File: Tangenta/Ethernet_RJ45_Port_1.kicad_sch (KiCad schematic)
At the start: 1 part, among them J5 HY911130A

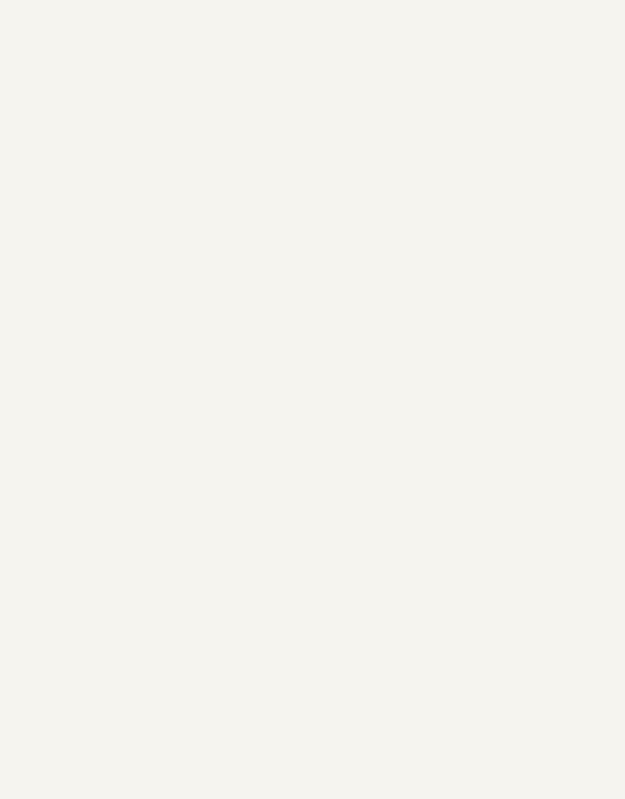
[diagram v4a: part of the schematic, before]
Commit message: Ethernet Switch schematic done, ports TBD...
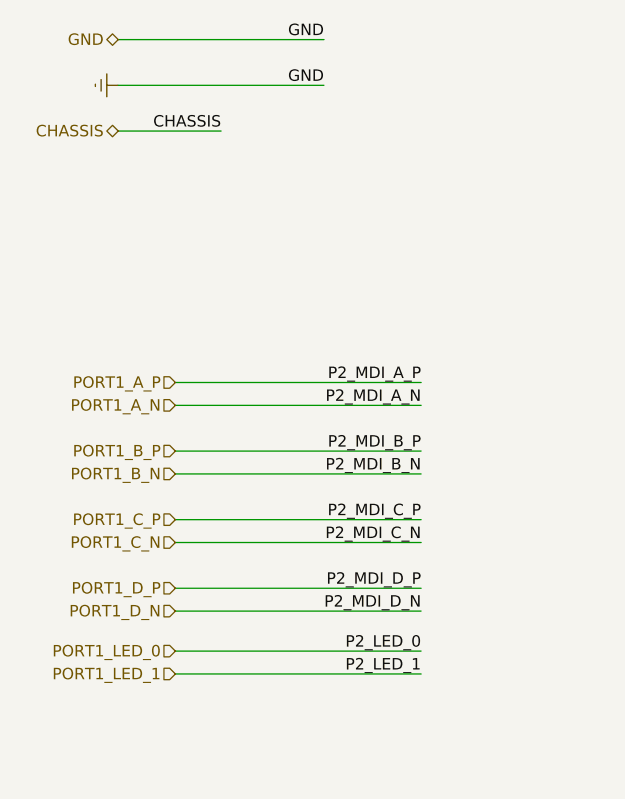
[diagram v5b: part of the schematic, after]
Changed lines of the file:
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@@
   (no_connect (at 134.62 75.565))
   (no_connect (at 160.02 73.025))
+  (wire (pts (xy 59.055 74.93) (xy 31.75 74.93))
+    (stroke (width 0) (type default))
+  )
+  (wire (pts (xy 25.4 29.21) (xy 36.83 29.21))
+    (stroke (width 0) (type default))
+  )
+  (wire (pts (xy 59.055 86.995) (xy 31.75 86.995))
+    (stroke (width 0) (type default))
+  )
+  (wire (pts (xy 48.26 24.13) (xy 25.4 24.13))
+    (stroke (width 0) (type default))
+  )
+  (wire (pts (xy 59.055 59.69) (xy 31.75 59.69))
+    (stroke (width 0) (type default))
+  )
+  (wire (pts (xy 59.055 89.535) (xy 31.75 89.535))
+    (stroke (width 0) (type default))
+  )
+  (wire (pts (xy 59.055 72.39) (xy 31.75 72.39))
+    (stroke (width 0) (type default))
+  )
+  (wire (pts (xy 59.055 80.01) (xy 31.75 80.01))
+    (stroke (width 0) (type default))
+  )
+  (wire (pts (xy 59.055 57.15) (xy 31.75 57.15))
+    (stroke (width 0) (type default))
+  )
+  (wire (pts (xy 59.055 82.55) (xy 31.75 82.55))
+    (stroke (width 0) (type default))
+  )
+  (wire (pts (xy 59.055 64.77) (xy 31.75 64.77))
+    (stroke (width 0) (type default))
+  )
+  (wire (pts (xy 48.26 19.05) (xy 25.4 19.05))
+    (stroke (width 0) (type default))
+  )
+  (wire (pts (xy 59.055 67.31) (xy 31.75 67.31))
+    (stroke (width 0) (type default))
+  )
+  (label "P2_MDI_C_P" (at 59.055 72.39 180) (fields_autoplaced)
+    (effects (font (size 1.27 1.27)) (justify right bottom))
+  )
+  (label "P2_LED_1" (at 59.055 89.535 180) (fields_autoplaced)
+    (effects (font (size 1.27 1.27)) (justify right bottom))
+  )
+  (label "P2_MDI_D_N" (at 59.055 82.55 180) (fields_autoplaced)
+    (effects (font (size 1.27 1.27)) (justify right bottom))
+  )
+  (label "P2_MDI_C_N" (at 59.055 74.93 180) (fields_autoplaced)
+    (effects (font (size 1.27 1.27)) (justify right bottom))
+  )
+  (label "P2_MDI_A_N" (at 59.055 59.69 180) (fields_autoplaced)
+    (effects (font (size 1.27 1.27)) (justify right bottom))
+  )
+  (label "P2_LED_0" (at 59.055 86.995 180) (fields_autoplaced)
+    (effects (font (size 1.27 1.27)) (justify right bottom))
+  )
+  (label "P2_MDI_D_P" (at 59.055 80.01 180) (fields_autoplaced)
+    (effects (font (size 1.27 1.27)) (justify right bottom))
+  )
+  (label "P2_MDI_A_P" (at 59.055 57.15 180) (fields_autoplaced)
+    (effects (font (size 1.27 1.27)) (justify right bottom))
+  )
+  (label "GND" (at 48.26 24.13 180) (fields_autoplaced)
+    (effects (font (size 1.27 1.27)) (justify right bottom))
+  )
+  (label "GND" (at 48.26 19.05 180) (fields_autoplaced)
+    (effects (font (size 1.27 1.27)) (justify right bottom))
+  )
+  (label "P2_MDI_B_P" (at 59.055 64.77 180) (fields_autoplaced)
+    (effects (font (size 1.27 1.27)) (justify right bottom))
+  )
+  (label "P2_MDI_B_N" (at 59.055 67.31 180) (fields_autoplaced)
+    (effects (font (size 1.27 1.27)) (justify right bottom))
+  )
+  (label "CHASSIS" (at 36.83 29.21 180) (fields_autoplaced)
+    (effects (font (size 1.27 1.27)) (justify right bottom))
+  )
+  (hierarchical_label "GND" (shape bidirectional) (at 25.4 19.05 180) (fields_autoplaced)
+    (effects (font (size 1.27 1.27)) (justify right))
+  )
+  (hierarchical_label "PORT1_D_N" (shape input) (at 31.75 82.55 180) (fields_autoplaced)
+    (effects (font (size 1.27 1.27)) (justify right))
+  )
+  (hierarchical_label "CHASSIS" (shape bidirectional) (at 25.4 29.21 180) (fields_autoplaced)
+    (effects (font (size 1.27 1.27)) (justify right))
+  )
+  (hierarchical_label "PORT1_D_P" (shape input) (at 31.75 80.01 180) (fields_autoplaced)
+    (effects (font (size 1.27 1.27)) (justify right))
+  )
+  (hierarchical_label "PORT1_A_N" (shape input) (at 31.75 59.69 180) (fields_autoplaced)
+    (effects (font (size 1.27 1.27)) (justify right))
+  )
+  (hierarchical_label "PORT1_C_P" (shape input) (at 31.75 72.39 180) (fields_autoplaced)
+    (effects (font (size 1.27 1.27)) (justify right))
+  )
+  (hierarchical_label "PORT1_A_P" (shape input) (at 31.75 57.15 180) (fields_autoplaced)
+    (effects (font (size 1.27 1.27)) (justify right))
+  )
+  (hierarchical_label "PORT1_LED_0" (shape input) (at 31.75 86.995 180) (fields_autoplaced)
+    (effects (font (size 1.27 1.27)) (justify right))
+  )
+  (hierarchical_label "PORT1_B_P" (shape input) (at 31.75 64.77 180) (fields_autoplaced)
+    (effects (font (size 1.27 1.27)) (justify right))
+  )
+  (hierarchical_label "PORT1_B_N" (shape input) (at 31.75 67.31 180) (fields_autoplaced)
+    (effects (font (size 1.27 1.27)) (justify right))
+  )
+  (hierarchical_label "PORT1_LED_1" (shape input) (at 31.75 89.535 180) (fields_autoplaced)
+    (effects (font (size 1.27 1.27)) (justify right))
+  )
+  (hierarchical_label "PORT1_C_N" (shape input) (at 31.75 74.93 180) (fields_autoplaced)
+    (effects (font (size 1.27 1.27)) (justify right))
+  )
+  (symbol (lib_id "power:GNDREF") (at 25.4 24.13 270) (mirror x) (unit 1)
+    (in_bom yes) (on_board yes) (dnp no) (fields_autoplaced)
+    (property "Reference" "#PWR013" (at 19.05 24.13 0)
+      (effects (font (size 1.27 1.27)) hide)
+    )
+    (property "Value" "GNDREF" (at 21.59 24.13 90)
+      (effects (font (size 1.27 1.27)) (justify right) hide)
+    )
+    (property "Footprint" "" (at 25.4 24.13 0)
+      (effects (font (size 1.27 1.27)) hide)
+    )
+    (property "Datasheet" "" (at 25.4 24.13 0)
+      (effects (font (size 1.27 1.27)) hide)
+    )
+    (pin "1")
+    (instances
+      (project "Tangenta"
+        (path "/358d1bcf-7599-4352-8c4d-baa18a5f09e6/d6c05402-162e-441f-bed8-be7996260fb4"
+          (reference "#PWR013") (unit 1)
+        )
+        (path "/358d1bcf-7599-4352-8c4d-baa18a5f09e6/9b1f6f94-444c-4c59-8de9-290bde336856"
+          (reference "#PWR050") (unit 1)
+        )
+        (path "/358d1bcf-7599-4352-8c4d-baa18a5f09e6/9b1f6f94-444c-4c59-8de9-290bde336856/04648235-6c5e-4915-ab80-8fea22048f3c"
+          (reference "#PWR050") (unit 1)
+        )
+        (path "/358d1bcf-7599-4352-8c4d-baa18a5f09e6/2bb52479-7b35-496d-9807-27e706c6ef7b"
+          (reference "#PWR059") (unit 1)
+        )
+        (path "/358d1bcf-7599-4352-8c4d-baa18a5f09e6/2bb52479-7b35-496d-9807-27e706c6ef7b/c653b84e-94ee-4be9-b47c-8c767f88973e"
+          (reference "#PWR059") (unit 1)
+        )
+        (path "/358d1bcf-7599-4352-8c4d-baa18a5f09e6/2bb52479-7b35-496d-9807-27e706c6ef7b/107b1895-3302-473d-bd1c-b123cf003d25"
+          (reference "#PWR065") (unit 1)
+        )
+      )
+    )
+  )
   (symbol (lib_id "RJ45_MAGJACK:HY911130A") (at 147.32 81.915 0) (unit 1)
     (in_bom yes) (on_board yes) (dnp no)

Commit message: Ethernet, current progress...
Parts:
- added C1: 100nF, Capacitor_SMD:C_0402_1005Metric, symbol Device:C_Small
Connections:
- net CHASSIS: now also J5.15 (SH), J5.16 (SH)
- net GNDREF: now also J5.10, J5.12, J5.13, C1.2
- net PORT1_A_N: now also J5.3
- net PORT1_A_P: now also J5.2
- net PORT1_B_N: now also J5.7
- net PORT1_B_P: now also J5.4
- net PORT1_C_N: now also J5.6
- net PORT1_C_P: now also J5.5
- net PORT1_D_N: now also J5.9
- net PORT1_D_P: now also J5.8
- net PORT1_LED_0: now also J5.11
- net PORT1_LED_1: now also J5.14
- net at J5.1: now also C1.1
- no-connect marks 16 -> 0

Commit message: Libraries exported from global to project.
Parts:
- C1: symbol Device:C_Small -> CholaSymbolsPrjLib:C_Small
- J5: symbol RJ45_MAGJACK:HY911130A -> CholaSymbolsPrjLib:HY911130A
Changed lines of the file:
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@@
     )
   )
-  (symbol (lib_id "Device:C_Small") (at 124.46 70.485 270) (unit 1)
+  (symbol (lib_id "CholaSymbolsPrjLib:C_Small") (at 124.46 70.485 270) (unit 1)
     (in_bom yes) (on_board yes) (dnp no)
     (property "Reference" "C1" (at 120.65 69.215 90)
@@
     )
   )
-  (symbol (lib_id "RJ45_MAGJACK:HY911130A") (at 147.32 81.915 0) (unit 1)
+  (symbol (lib_id "CholaSymbolsPrjLib:HY911130A") (at 147.32 81.915 0) (unit 1)
     (in_bom yes) (on_board yes) (dnp no)
     (property "Reference" "J5" (at 147.32 63.754 0)
